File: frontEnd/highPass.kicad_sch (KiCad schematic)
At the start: 15 parts, among them U101 BGS12P2L6E6327XTSA1, U102 BGS12P2L6E6327XTSA1

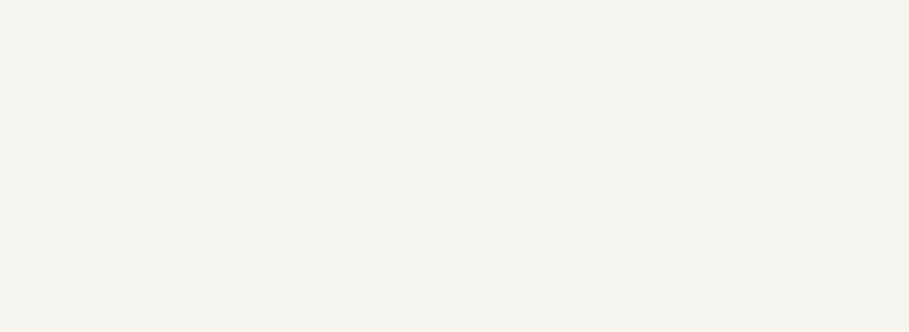
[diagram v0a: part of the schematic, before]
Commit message: update schematics, add bypass for the attenuator
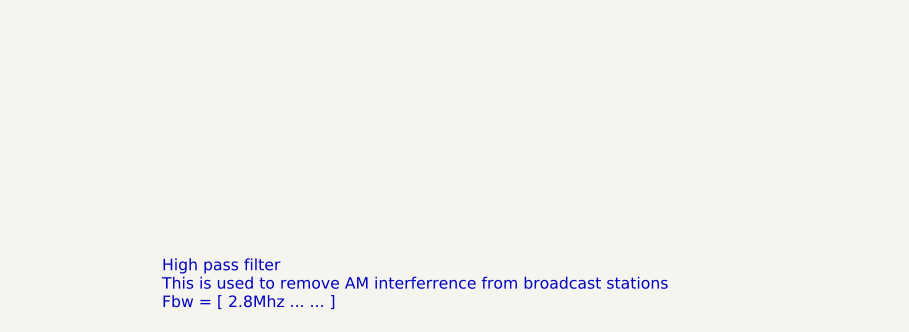
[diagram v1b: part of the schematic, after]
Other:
- note added: "High pass filter This is used to remove AM interferrence from broadcast stations Fbw = [ 2.8Mhz ... ... ]"
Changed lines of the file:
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@@
     (stroke (width 0) (type default) (color 0 0 0 0))
+  )
+  (text "High pass filter\nThis is used to remove AM interferrence from broadcast stations\nFbw = [ 2.8Mhz ... ... ]"
+    (at 179.07 175.26 0)
+    (effects (font (size 1.27 1.27)) (justify left bottom))
   )
   (hierarchical_label "RF_IN" (shape input) (at 57.15 83.82 180)

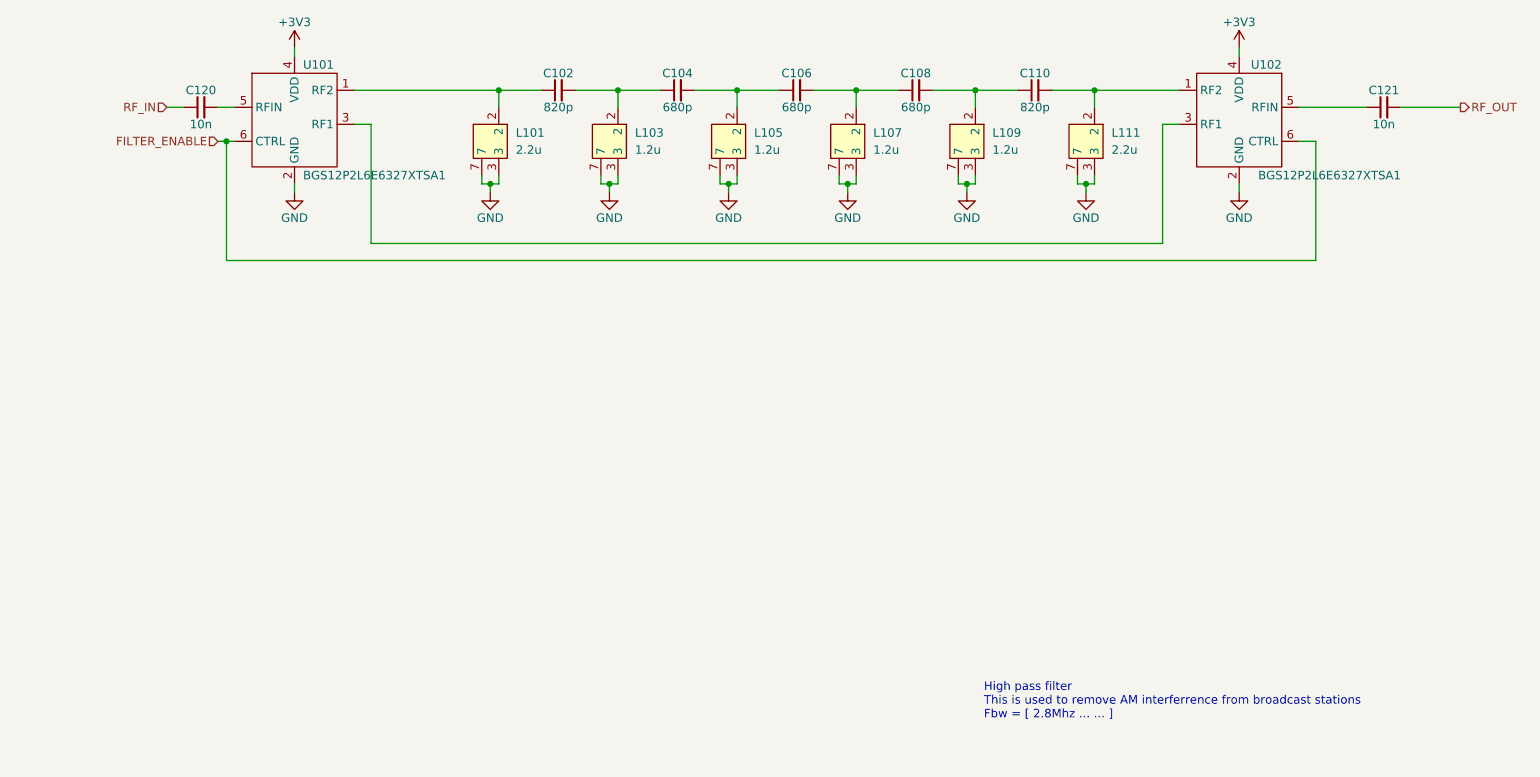
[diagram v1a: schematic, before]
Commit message: simply schematic: remove attenuator and gain blocks; add 5 way multiplexer
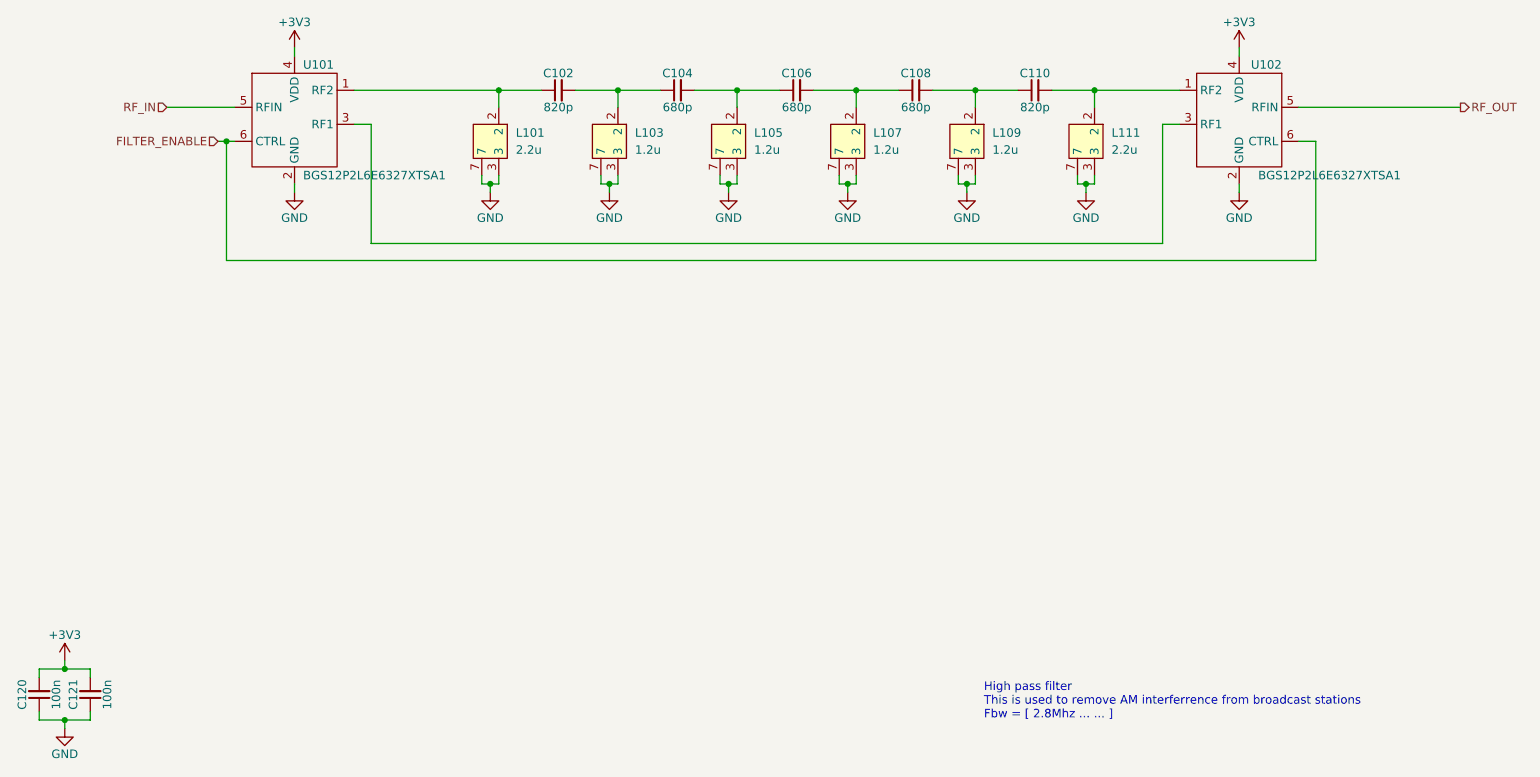
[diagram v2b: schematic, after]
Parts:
- C120, C121: value 10n -> 100n
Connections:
- net +3V3: now also C120.2, C121.2
- net GND: now also C120.1, C121.1
- net RF_IN: now also U101.5 (RFIN); no longer C120.1
- net RF_OUT: now also U102.5 (RFIN); no longer C121.2
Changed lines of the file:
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@@
   (junction (at 106.68 81.28) (diameter 0) (color 0 0 0 0)
   )
+  (junction (at 41.91 175.26) (diameter 0) (color 0 0 0 0)
+  )
   (junction (at 124.46 81.28) (diameter 0) (color 0 0 0 0)
   )
   (junction (at 177.8 81.28) (diameter 0) (color 0 0 0 0)
   )
+  (junction (at 41.91 167.64) (diameter 0) (color 0 0 0 0)
+  )
   (junction (at 66.04 88.9) (diameter 0) (color 0 0 0 0)
   )
@@
   (junction (at 160.02 81.28) (diameter 0) (color 0 0 0 0)
   )
+  (wire (pts (xy 41.91 175.26) (xy 41.91 176.53))
+    (stroke (width 0) (type default) (color 0 0 0 0))
+  )
+  (wire (pts (xy 38.1 175.26) (xy 41.91 175.26))
+    (stroke (width 0) (type default) (color 0 0 0 0))
+  )
   (wire (pts (xy 140.97 95.25) (xy 142.24 95.25))
     (stroke (width 0) (type default) (color 0 0 0 0))
@@
     (stroke (width 0) (type default) (color 0 0 0 0))
   )
+  (wire (pts (xy 45.72 173.99) (xy 45.72 175.26))
+    (stroke (width 0) (type default) (color 0 0 0 0))
+  )
   (wire (pts (xy 124.46 81.28) (xy 130.81 81.28))
     (stroke (width 0) (type default) (color 0 0 0 0))
@@
     (stroke (width 0) (type default) (color 0 0 0 0))
   )
+  (wire (pts (xy 41.91 175.26) (xy 45.72 175.26))
+    (stroke (width 0) (type default) (color 0 0 0 0))
+  )
   (wire (pts (xy 106.68 81.28) (xy 113.03 81.28))
     (stroke (width 0) (type default) (color 0 0 0 0))
@@
     (stroke (width 0) (type default) (color 0 0 0 0))
   )
+  (wire (pts (xy 38.1 167.64) (xy 41.91 167.64))
+    (stroke (width 0) (type default) (color 0 0 0 0))
+  )
   (wire (pts (xy 87.63 86.36) (xy 87.63 104.14))
     (stroke (width 0) (type default) (color 0 0 0 0))
@@
     (stroke (width 0) (type default) (color 0 0 0 0))
   )
-  (wire (pts (xy 57.15 83.82) (xy 59.69 83.82))
-    (stroke (width 0) (type default) (color 0 0 0 0))
-  )
   (wire (pts (xy 176.53 95.25) (xy 177.8 95.25))
     (stroke (width 0) (type default) (color 0 0 0 0))
@@
     (stroke (width 0) (type default) (color 0 0 0 0))
   )
-  (wire (pts (xy 64.77 83.82) (xy 67.31 83.82))
+  (wire (pts (xy 45.72 167.64) (xy 45.72 168.91))
+    (stroke (width 0) (type default) (color 0 0 0 0))
+  )
+  (wire (pts (xy 57.15 83.82) (xy 67.31 83.82))
     (stroke (width 0) (type default) (color 0 0 0 0))
   )
@@
     (stroke (width 0) (type default) (color 0 0 0 0))
   )
+  (wire (pts (xy 38.1 173.99) (xy 38.1 175.26))
+    (stroke (width 0) (type default) (color 0 0 0 0))
+  )
   (wire (pts (xy 157.48 93.98) (xy 157.48 95.25))
     (stroke (width 0) (type default) (color 0 0 0 0))
@@
     (stroke (width 0) (type default) (color 0 0 0 0))
   )
+  (wire (pts (xy 38.1 168.91) (xy 38.1 167.64))
+    (stroke (width 0) (type default) (color 0 0 0 0))
+  )
   (wire (pts (xy 140.97 95.25) (xy 140.97 96.52))
     (stroke (width 0) (type default) (color 0 0 0 0))
@@
     (stroke (width 0) (type default) (color 0 0 0 0))
   )
+  (wire (pts (xy 41.91 167.64) (xy 45.72 167.64))
+    (stroke (width 0) (type default) (color 0 0 0 0))
+  )
   (wire (pts (xy 193.04 93.98) (xy 193.04 95.25))
     (stroke (width 0) (type default) (color 0 0 0 0))
@@
     (stroke (width 0) (type default) (color 0 0 0 0))
   )
-  (wire (pts (xy 241.3 83.82) (xy 250.19 83.82))
-    (stroke (width 0) (type default) (color 0 0 0 0))
-  )
   (wire (pts (xy 123.19 95.25) (xy 123.19 96.52))
     (stroke (width 0) (type default) (color 0 0 0 0))
   )
-  (wire (pts (xy 226.06 83.82) (xy 236.22 83.82))
+  (wire (pts (xy 226.06 83.82) (xy 250.19 83.82))
     (stroke (width 0) (type default) (color 0 0 0 0))
   )
   (wire (pts (xy 121.92 95.25) (xy 123.19 95.25))
+    (stroke (width 0) (type default) (color 0 0 0 0))
+  )
+  (wire (pts (xy 41.91 166.37) (xy 41.91 167.64))
     (stroke (width 0) (type default) (color 0 0 0 0))
   )
@@
     (effects (font (size 1.27 1.27)) (justify right))
   )
+  (symbol (lib_id "Device:C_Small") (at 45.72 171.45 180) (unit 1)
+    (in_bom yes) (on_board yes)
+    (property "Reference" "C121" (id 0) (at 43.18 171.45 90))
+    (property "Value" "100n" (id 1) (at 48.26 171.45 90))
+    (property "Footprint" "Capacitor_SMD:C_0805_2012Metric" (id 2) (at 45.72 171.45 0)
+      (effects (font (size 1.27 1.27)) hide)
+    )
+    (property "Datasheet" "~" (id 3) (at 45.72 171.45 0)
+      (effects (font (size 1.27 1.27)) hide)
+    )
+    (pin "1")
+    (pin "2")
+  )
   (symbol (lib_id "power:GND") (at 105.41 96.52 0) (unit 1)
     (in_bom yes) (on_board yes)
@@
     )
     (property "Datasheet" "" (id 3) (at 105.41 96.52 0)
+      (effects (font (size 1.27 1.27)) hide)
+    )
+    (pin "1")
+  )
+  (symbol (lib_id "power:+3V3") (at 41.91 166.37 0) (unit 1)
+    (in_bom yes) (on_board yes)
+    (property "Reference" "#PWR?" (id 0) (at 41.91 170.18 0)
+      (effects (font (size 1.27 1.27)) hide)
+    )
+    (property "Value" "+3V3" (id 1) (at 41.91 162.56 0))
+    (property "Footprint" "" (id 2) (at 41.91 166.37 0)
+      (effects (font (size 1.27 1.27)) hide)
+    )
+    (property "Datasheet" "" (id 3) (at 41.91 166.37 0)
       (effects (font (size 1.27 1.27)) hide)
     )
@@
     (pin "7")
   )
+  (symbol (lib_id "Device:C_Small") (at 38.1 171.45 180) (unit 1)
+    (in_bom yes) (on_board yes)
+    (property "Reference" "C120" (id 0) (at 35.56 171.45 90))
+    (property "Value" "100n" (id 1) (at 40.64 171.45 90))
+    (property "Footprint" "Capacitor_SMD:C_0805_2012Metric" (id 2) (at 38.1 171.45 0)
+      (effects (font (size 1.27 1.27)) hide)
+    )
+    (property "Datasheet" "~" (id 3) (at 38.1 171.45 0)
+      (effects (font (size 1.27 1.27)) hide)
+    )
+    (pin "1")
+    (pin "2")
+  )
   (symbol (lib_id "Device:C_Small") (at 133.35 81.28 90) (unit 1)
     (in_bom yes) (on_board yes)
@@
     (pin "2")
   )
+  (symbol (lib_id "power:GND") (at 41.91 176.53 0) (unit 1)
+    (in_bom yes) (on_board yes)
+    (property "Reference" "#PWR?" (id 0) (at 41.91 182.88 0)
+      (effects (font (size 1.27 1.27)) hide)
+    )
+    (property "Value" "GND" (id 1) (at 41.91 180.34 0))
+    (property "Footprint" "" (id 2) (at 41.91 176.53 0)
+      (effects (font (size 1.27 1.27)) hide)
+    )
+    (property "Datasheet" "" (id 3) (at 41.91 176.53 0)
+      (effects (font (size 1.27 1.27)) hide)
+    )
+    (pin "1")
+  )
   (symbol (lib_id "frontEnd:TOKO_10K") (at 195.58 88.9 270) (unit 1)
     (in_bom yes) (on_board yes) (fields_autoplaced)
@@
     (pin "7")
   )
-  (symbol (lib_id "Device:C_Small") (at 62.23 83.82 90) (unit 1)
-    (in_bom yes) (on_board yes)
-    (property "Reference" "C120" (id 0) (at 62.23 81.28 90))
-    (property "Value" "10n" (id 1) (at 62.23 86.36 90))
-    (property "Footprint" "Capacitor_SMD:C_0805_2012Metric" (id 2) (at 62.23 83.82 0)
-      (effects (font (size 1.27 1.27)) hide)
-    )
-    (property "Datasheet" "~" (id 3) (at 62.23 83.82 0)
-      (effects (font (size 1.27 1.27)) hide)
-    )
-    (pin "1")
-    (pin "2")
-  )
-  (symbol (lib_id "Device:C_Small") (at 238.76 83.82 90) (unit 1)
-    (in_bom yes) (on_board yes)
-    (property "Reference" "C121" (id 0) (at 238.76 81.28 90))
-    (property "Value" "10n" (id 1) (at 238.76 86.36 90))
-    (property "Footprint" "Capacitor_SMD:C_0805_2012Metric" (id 2) (at 238.76 83.82 0)
-      (effects (font (size 1.27 1.27)) hide)
-    )
-    (property "Datasheet" "~" (id 3) (at 238.76 83.82 0)
-      (effects (font (size 1.27 1.27)) hide)
-    )
-    (pin "1")
-    (pin "2")
-  )
   (symbol (lib_id "power:+3V3") (at 76.2 74.93 0) (unit 1)
